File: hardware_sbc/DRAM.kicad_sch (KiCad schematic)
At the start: 38 parts, among them U1 IMX8MM, U3 MT53E256M32D2DS-053 WT:B

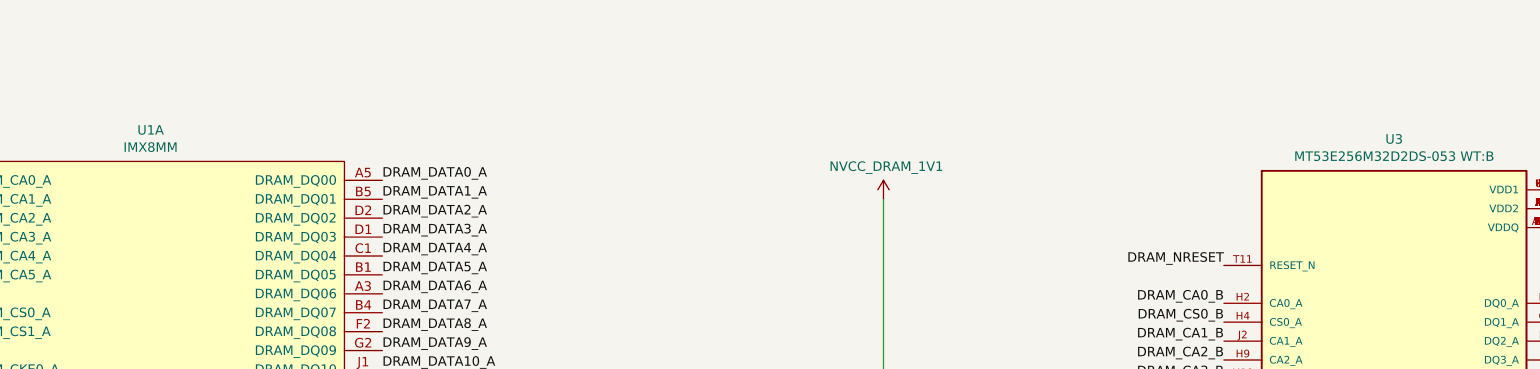
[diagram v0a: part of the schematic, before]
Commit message: Updated production files and fixed schematic link issue.
Fixed schematic unit number issue and re-linked to PCB.
New gerbers, STEP file, schematic PDF.
Deleted old KiCAD 6 files.
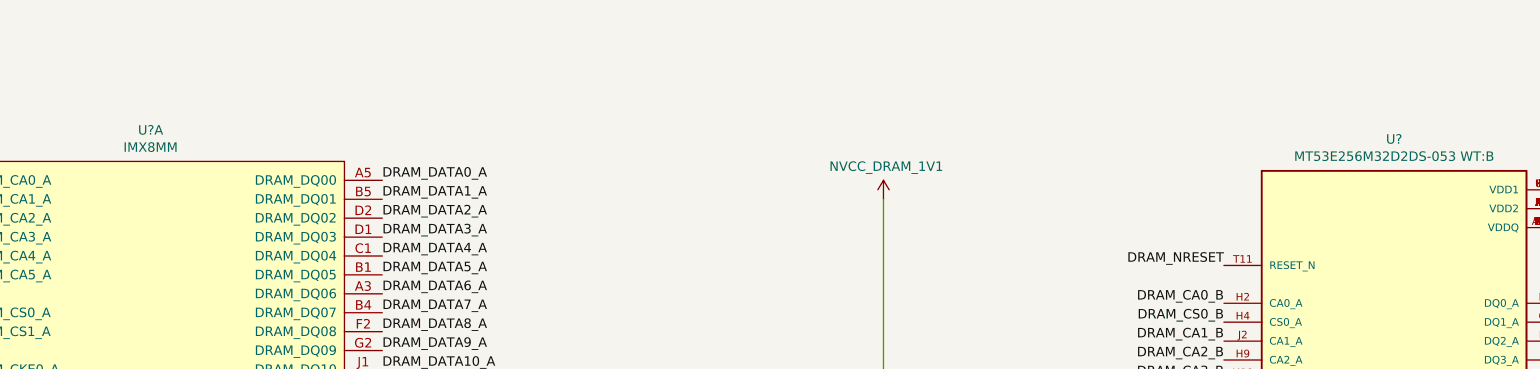
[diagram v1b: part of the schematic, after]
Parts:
- renumbered U3 to U?, U1 to U?
